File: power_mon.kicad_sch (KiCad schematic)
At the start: 16 parts, among them IC1 LT3960EMSE#TRPBF, U1 INA228, U2 INA228

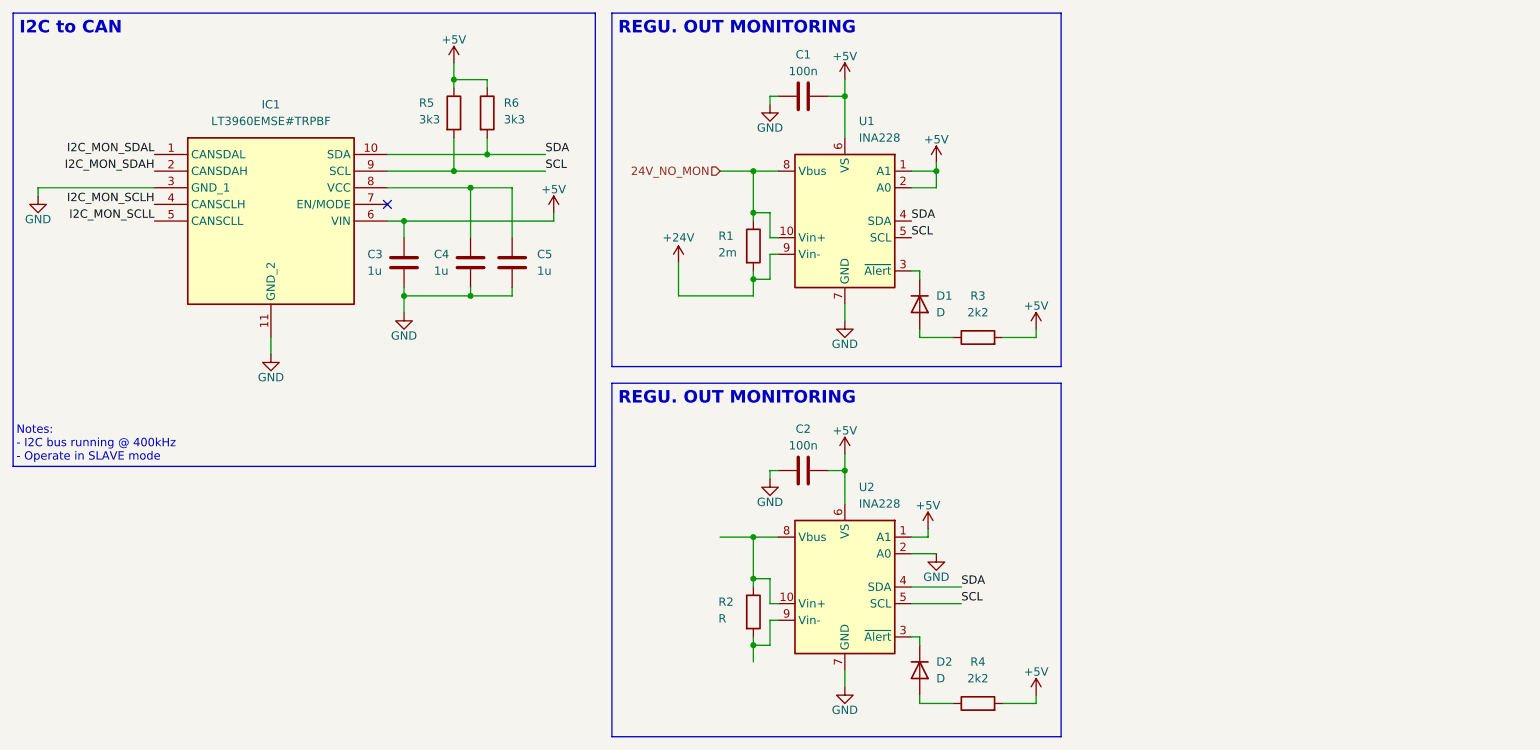
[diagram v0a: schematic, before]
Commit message: add: regulator + monitoring
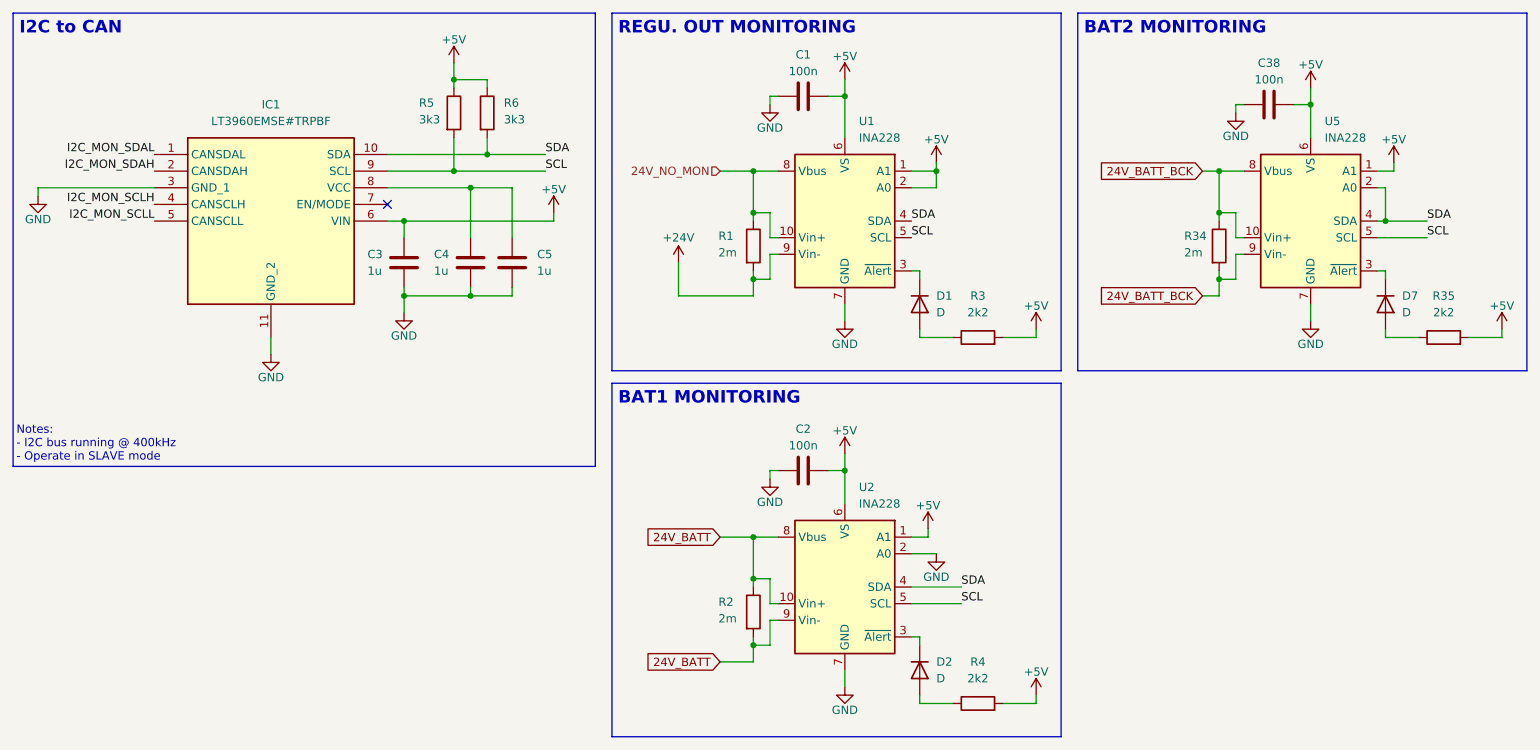
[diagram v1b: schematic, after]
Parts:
- added C38: 100n, symbol Device:C
- added D7: D, symbol Device:D
- added R34: 2m, symbol Device:R
- added R35: 2k2, symbol Device:R
- added U5: INA228, Package_SO:VSSOP-10_3x3mm_P0.5mm, symbol Sensor_Energy:INA228
- R2: value R -> 2m
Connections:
- net +5V: now also C38.2, R35.2, U5.1 (A1), U5.6 (VS)
- net GND: now also C38.1, U5.7 (GND)
- net SCL: now also U5.5 (SCL)
- net SDA: now also U5.2 (A0), U5.4 (SDA)
- net 24V_BATT: now reaches R2.1, U2.10 (Vin+), U2.8 (Vbus)
- net 24V_BATT: now also R2.2, U2.9 (Vin-)
- new net: D7.2 (A), R35.1
- new net: D7.1 (K), U5.3 (~{Alert})
- new net 24V_BATT_BCK: R34.1, R34.2, U5.10 (Vin+), U5.8 (Vbus), U5.9 (Vin-)
